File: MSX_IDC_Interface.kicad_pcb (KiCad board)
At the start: 2 copper layers, 103 x 66 mm, 26 parts, among them J1 DE1 GPIO, Q1 2N2222, Q2 2N2222, U1 74LVC245A, U2 74LVC245A, U3 74LVC245A, U4 74LVC245A, U5 74LVC245A, U6 74LS00

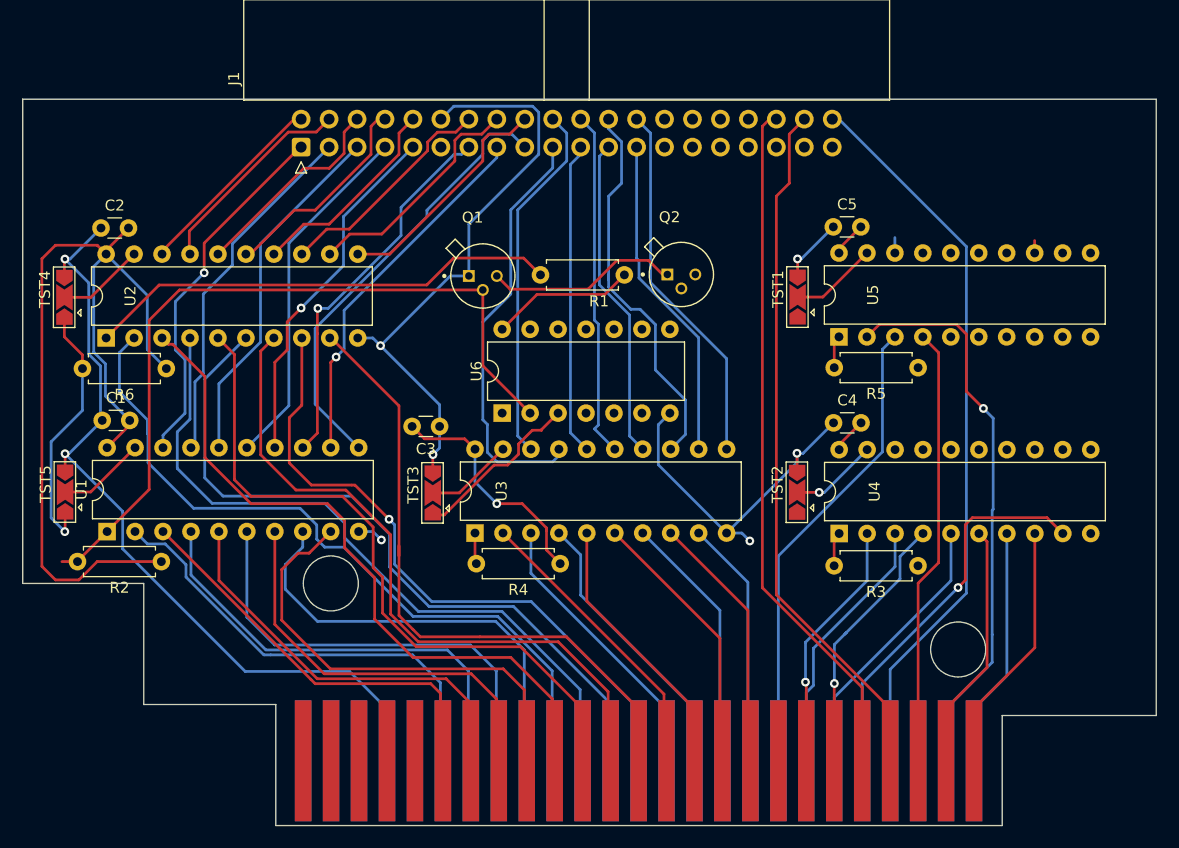
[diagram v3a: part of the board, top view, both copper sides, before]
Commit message: Finished routing. Rules chekc not done yet
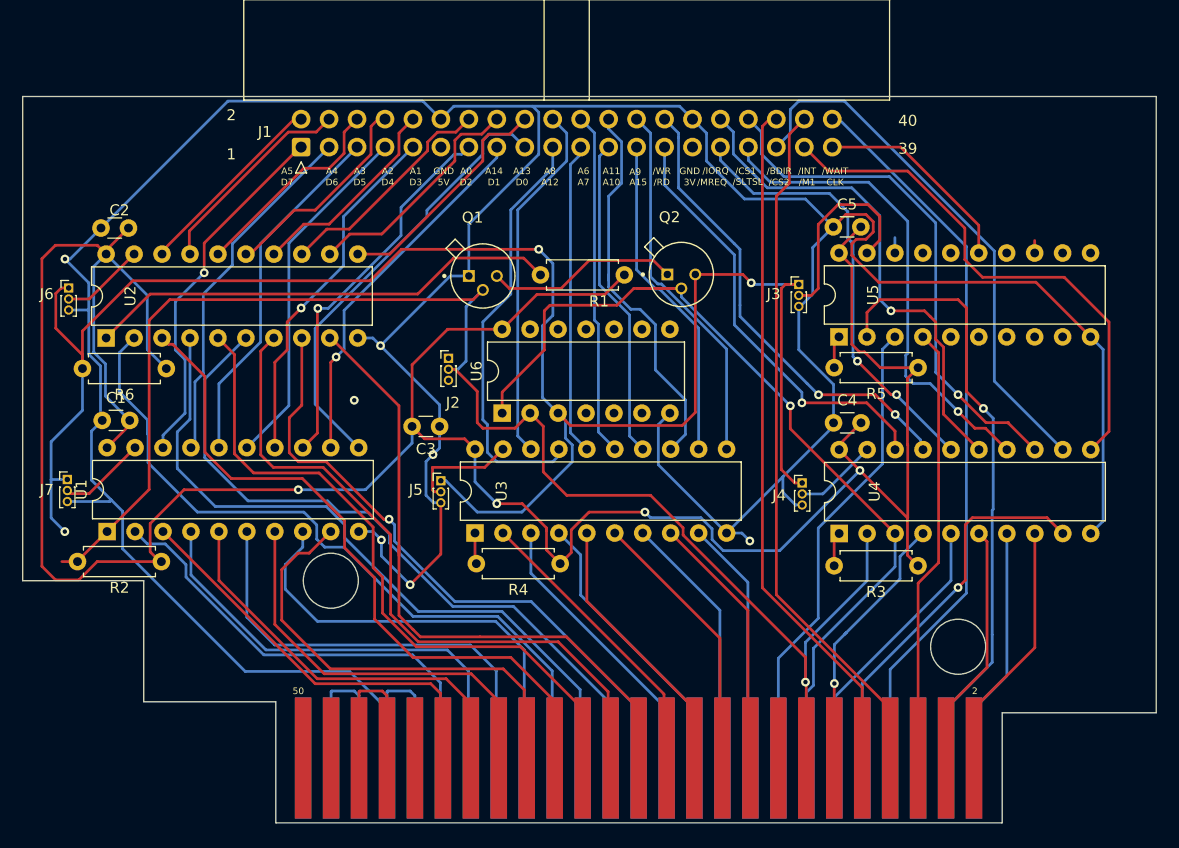
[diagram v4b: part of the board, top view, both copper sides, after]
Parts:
- removed TST1, TST2, TST3, TST4, TST5: SolderJumper_3_Open, Jumper:SolderJumper-3_P2.0mm_Open_TrianglePad1.0x1.5mm
- added J2: Conn_01x03_Male, Connector_PinHeader_1.00mm:PinHeader_1x03_P1.00mm_Vertical, F.Cu at (90.9, 43.9)
- added J3: Conn_01x03_Male, Connector_PinHeader_1.00mm:PinHeader_1x03_P1.00mm_Vertical, F.Cu at (122.7, 37.2)
- added J4: Conn_01x03_Male, Connector_PinHeader_1.00mm:PinHeader_1x03_P1.00mm_Vertical, F.Cu at (123.0, 55.3)
- added J5: Conn_01x03_Male, Connector_PinHeader_1.00mm:PinHeader_1x03_P1.00mm_Vertical, F.Cu at (90.2, 55.1)
- added J6: Conn_01x03_Male, Connector_PinHeader_1.00mm:PinHeader_1x03_P1.00mm_Vertical, F.Cu at (56.3, 37.6)
- added J7: Conn_01x03_Male, Connector_PinHeader_1.00mm:PinHeader_1x03_P1.00mm_Vertical, F.Cu at (56.2, 55.0)
- moved CONN1 0.25 mm to (101.8, 50.7)
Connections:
- net Net-(CONN1-Pad44) renamed SW1
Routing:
- net GNDREF: track 167.9 -> 339.8 mm, vias 8 -> 6
- net Net-(Q2-Pad3): track 39.1 -> 168.0 mm, vias 1 -> 3
- net +3.3V: track 124.3 -> 250.4 mm, vias 1 -> 4
- net /WR: track 24.0 -> 82.5 mm, vias 0 -> 1
- net /C_CS2: track 0.00 -> 49.1 mm
- net /C_M1: track 0.00 -> 48.2 mm
- net /C_CS1: track 0.00 -> 47.6 mm, vias 0 -> 1
- net /RD: track 93.5 -> 140.7 mm
- net /C_IORQ: track 0.00 -> 46.1 mm, vias 0 -> 1
- net /C_SLTSL: track 0.00 -> 44.1 mm, vias 0 -> 1
- net /C_WR: track 0.00 -> 42.8 mm, vias 0 -> 2
- net /C_MREQ: track 0.00 -> 40.5 mm, vias 0 -> 2
- net /C_RD: track 0.00 -> 39.6 mm, vias 0 -> 1
- net C_CLOCK: track 0.00 -> 18.8 mm
- net SW1: track 0.00 -> 14.9 mm
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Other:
- board text added: "/BDIR"
- board text added: "/CS1"
- board text added: "/CS2"
- board text added: "/INT"
- board text added: "/IORQ"
- board text added: "/M1"
- board text added: "/MREQ"
- board text added: "/RD"
- board text added: "/SLTSL"
- board text added: "/WAIT"
- board text added: "/WR"
- board text added: "1"
- board text added: "2"
- board text added: "39"
- board text added: "3V"
- board text added: "40"
- board text added: "49"
- board text added: "50"
- board text added: "5V"
- board text added: "A0"
- board text added: "A1"
- board text added: "A10"
- board text added: "A11"
- board text added: "A12"
- board text added: "A13"
- board text added: "A14"
- board text added: "A15"
- board text added: "A2"
- board text added: "A3"
- board text added: "A4"
- board text added: "A5"
- board text added: "A6"
- board text added: "A7"
- board text added: "A8"
- board text added: "A9"
- board text added: "CLK"
- board text added: "D0"
- board text added: "D1"
- board text added: "D2"
- board text added: "D3"
- board text added: "D4"
- board text added: "D5"
- board text added: "D6"
- board text added: "D7"
- board text added: "GND"

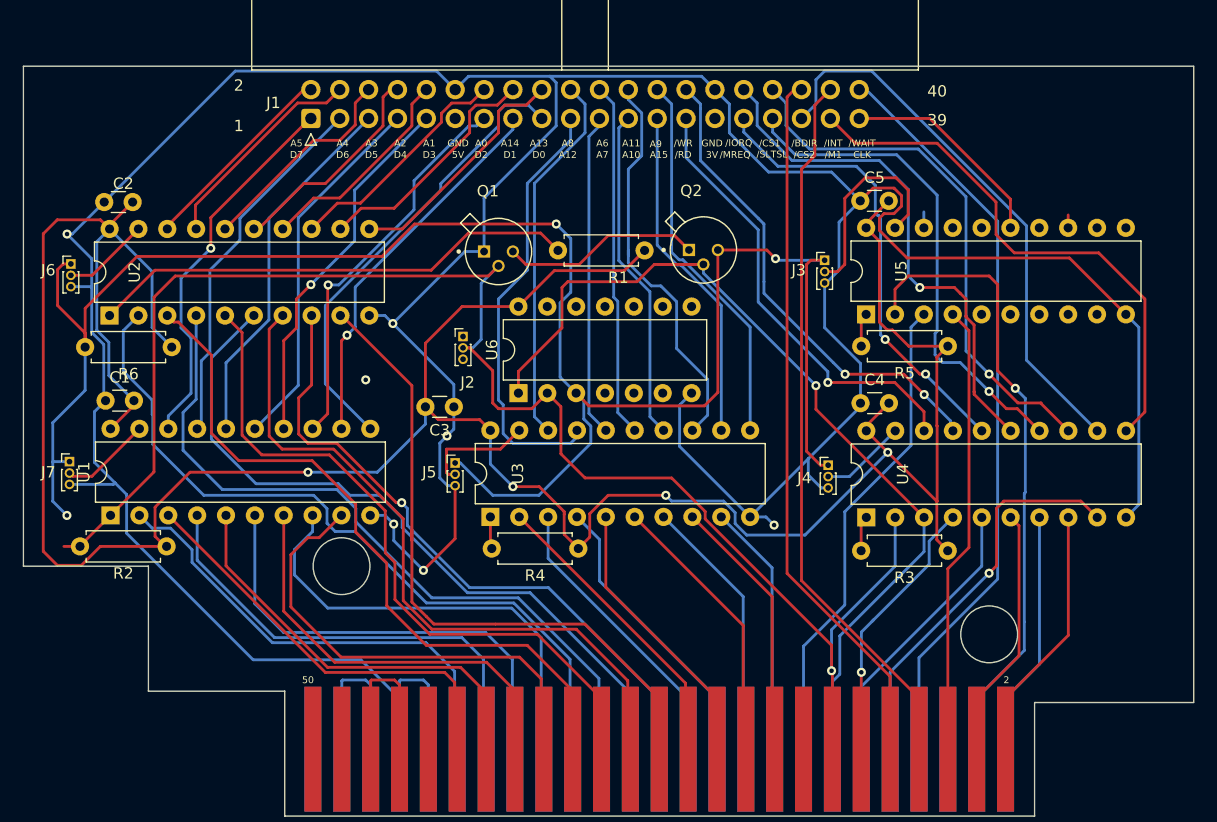
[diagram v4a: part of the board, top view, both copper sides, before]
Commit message: Resolvig clearance issues - wip
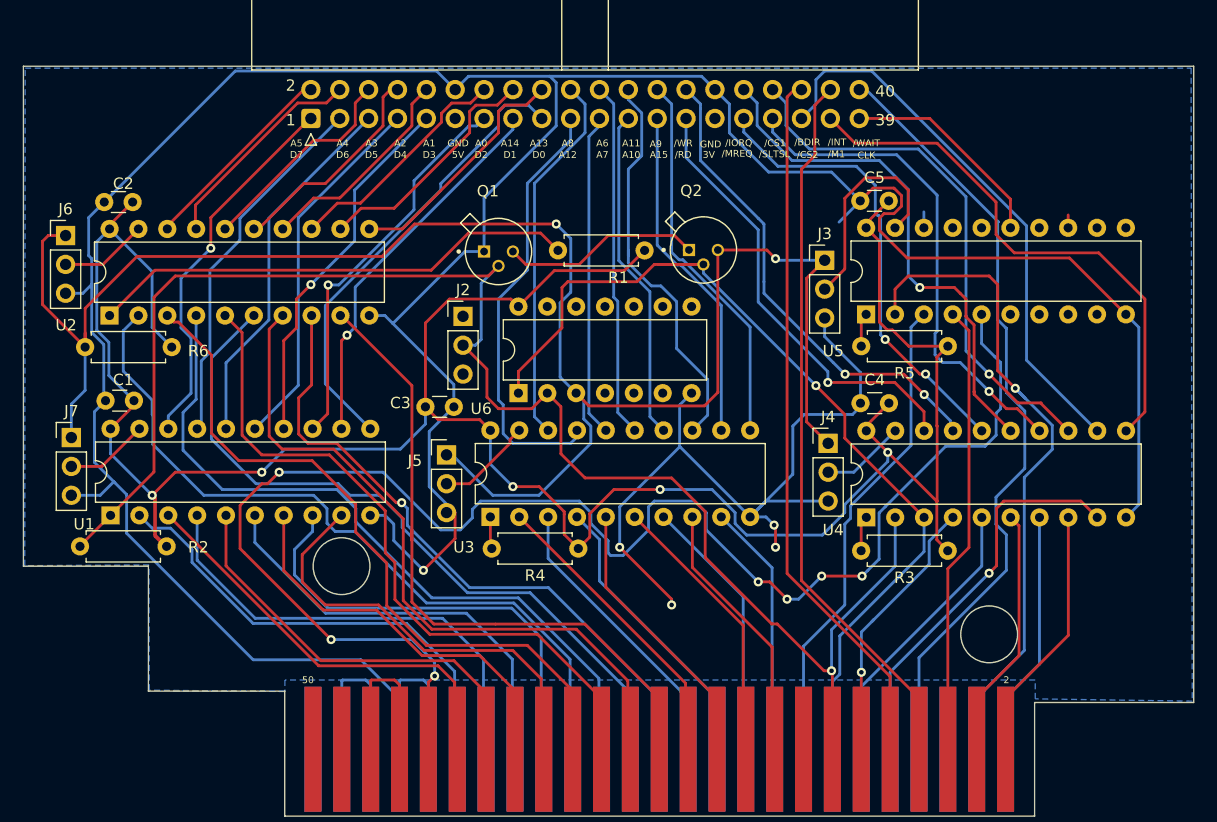
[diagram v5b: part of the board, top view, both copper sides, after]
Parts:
- J2, J3, J4, J5, J6, J7: footprint Connector_PinHeader_1.00mm:PinHeader_1x03_P1.00mm_Vertical -> Connector_PinHeader_2.54mm:PinHeader_1x03_P2.54mm_Vertical
- moved J6 2.54 mm to (55.9, 35.1)
- moved J7 2.13 mm to (56.4, 52.8)
- moved J4 1.92 mm to (123.0, 53.3)
- moved J2 1.77 mm to (90.9, 42.2)
- moved J5 1.04 mm to (89.4, 54.4)
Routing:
- net CLOCK: track 0.00 -> 135.0 mm, vias 0 -> 7
- net +3.3V: track 250.4 -> 219.1 mm, vias 4 -> 5
- net GNDREF: track 339.8 -> 357.1 mm, vias 6 -> 5
- net Net-(Q2-Pad3): track 168.0 -> 161.5 mm, vias 3 -> 2
- net D0: track 41.4 -> 38.1 mm
- net /CS12: track 56.2 -> 59.4 mm
- net D3: track 40.4 -> 37.3 mm
- net /WAIT: track 66.6 -> 69.4 mm
- net D2: track 36.8 -> 34.7 mm
- net Net-(U3-Pad19): track 9.97 -> 8.54 mm
- net /RD: track 140.7 -> 139.8 mm
- net Net-(U5-Pad19): track 18.4 -> 19.3 mm
- net Net-(U2-Pad19): track 7.63 -> 8.38 mm
- net (no net): vias 1 -> 0
- added copper zone on B.Cu, net GNDREF

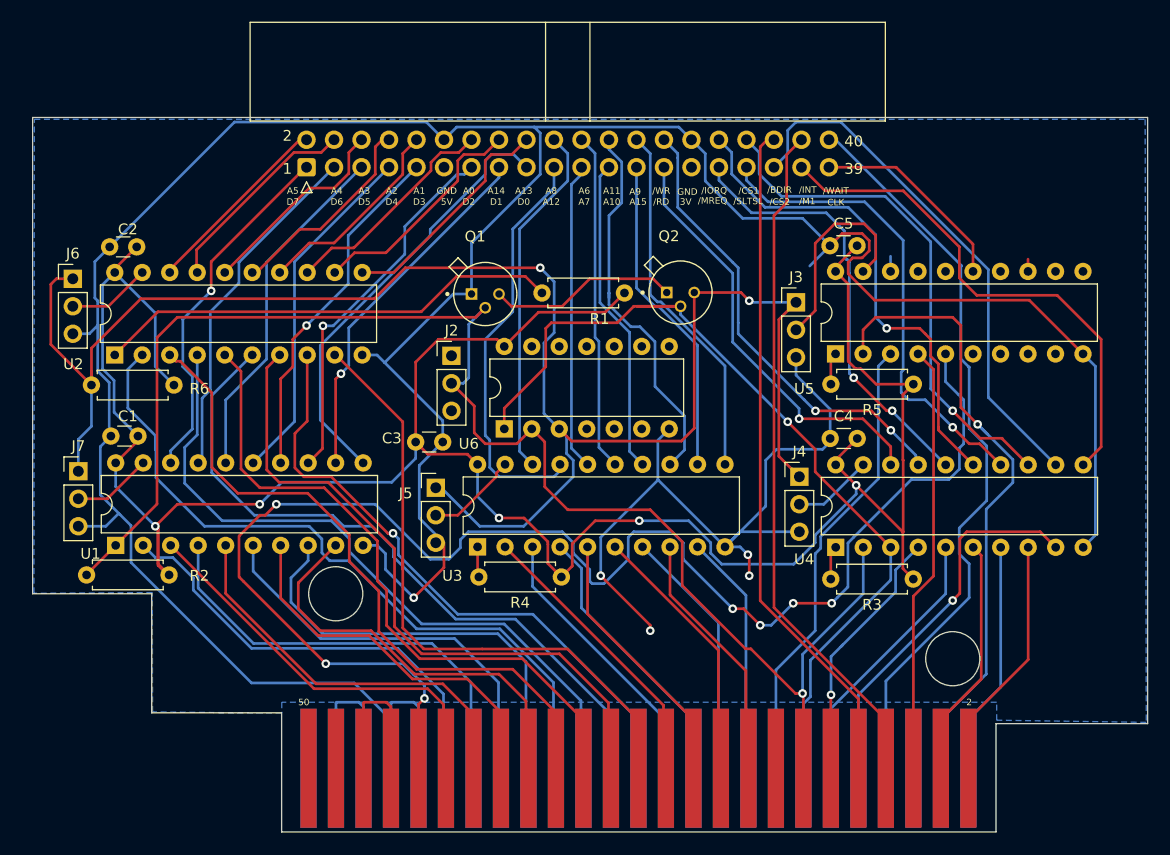
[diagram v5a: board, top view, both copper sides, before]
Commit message: Changed NAND gate for XNOR gate (bug); Completed routing
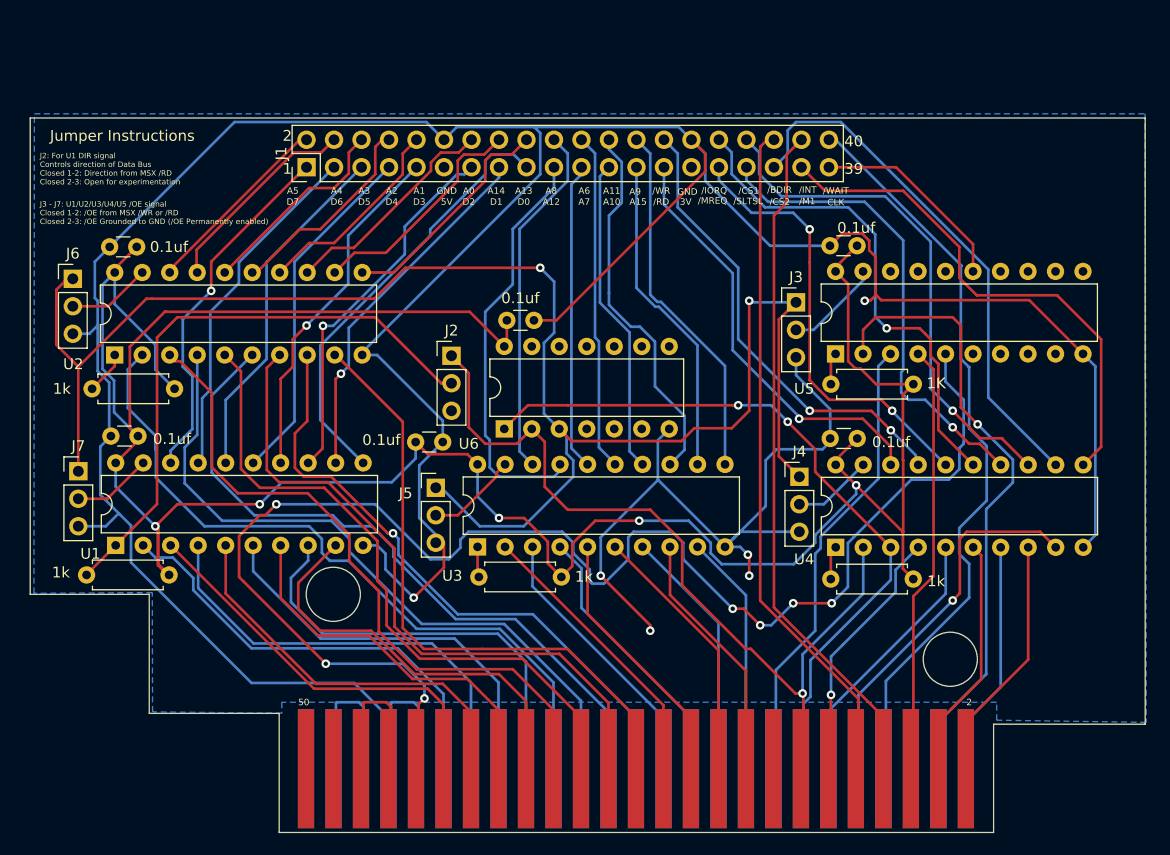
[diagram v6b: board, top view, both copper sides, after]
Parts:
- removed Q1, Q2: 2N2222, Roni Footprints:TO127P584H533-3
- removed R6: 1k, Resistor_THT:R_Axial_DIN0207_L6.3mm_D2.5mm_P7.62mm_Horizontal
- added C6: 0.1uf, Capacitor_THT:C_Disc_D3.0mm_W1.6mm_P2.50mm, F.Cu at (98.5, 38.9)
- J1: footprint Connector_IDC:IDC-Header_2x20_P2.54mm_Horizontal -> Connector_PinHeader_2.54mm:PinHeader_2x20_P2.54mm_Vertical
- R5: value 1k -> 1K
- U6: value 74LS00 -> 4077
- moved R1 42.5 mm to (65.3, 45.2)
- moved CONN1 0.23 mm to (101.6, 50.8)
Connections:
- J2 pad 1: unconnected-(J2-Pad1) -> /RD
- J2 pad 2: /RD -> Net-(J2-Pad2)
- R2 pad 2: /RD -> Net-(J2-Pad2)
- U1 pad 1: /RD -> Net-(J2-Pad2)
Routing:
- net /RD: track 139.8 -> 77.2 mm
- net Net-(J2-Pad2): track 0.00 -> 55.1 mm
- net Net-(R1-Pad2): track 43.1 -> 3.99 mm
- net GNDREF: track 357.1 -> 377.0 mm, vias 5 -> 6
- net +3.3V: track 219.1 -> 237.9 mm
- net Net-(Q1-Pad3): track 18.0 -> 0.00 mm
- net /WR: track 82.5 -> 67.3 mm, vias 1 -> 2
- net Net-(J3-Pad2): track 19.3 -> 9.04 mm
- net Net-(J3-Pad1): track 161.5 -> 154.8 mm
- net /CS12: track 59.4 -> 57.9 mm
- net /C_CS12: track 1.40 -> 0.00 mm
- net unconnected-(U5-Pad13): track 1.13 -> 0.00 mm
- net /C_MREQ: track 40.5 -> 41.2 mm
- net Net-(J6-Pad2): track 8.38 -> 7.70 mm
- net /RFSH: track 40.5 -> 39.9 mm
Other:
- board text added: "J2: For U1 DIR signal Controls direction of Data Bus Closed 1-2: Direction from MSX /RD Closed 2-3: Open for experimentation"
- board text added: "J3 - J7: U1/U2/U3/U4/U5 /OE signal Closed 1-2: /OE from MSX /WR or /RD Closed 2-3: /OE Grounded to GND (/OE Permanently enabled)"
- board text added: "Jumper Instructions"

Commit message: Resistors changed to 2.2k and routing completed
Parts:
- R1, R2, R3, R4: value 1k -> 2.2K
- R5: value 1K -> 2.2K
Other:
- board text added: "J2: U1 DIR signal Closed 1-2: Direction from MSX /RD Closed 2-3: Open for experimentation"
- board text removed: "J2: For U1 DIR signal Controls direction of Data Bus Closed 1-2: Direction from MSX /RD Closed 2-3: Open for experimentation"
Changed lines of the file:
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@@
     (property "Sheetname" "")
     (attr through_hole)
-    (fp_text reference "J1" (at 1.27 -2.33 90) (layer "F.SilkS")
+    (fp_text reference "J1" (at 1.27 -2.33 90) (layer "F.SilkS") hide
       (effects (font (size 1 1) (thickness 0.15)))
     )
@@
       (effects (font (size 1 1) (thickness 0.15)))
     )
-    (fp_text value "1k" (at -2.087435 0.027176) (layer "F.SilkS")
+    (fp_text value "2.2K" (at -3.131533 -0.90199) (layer "F.SilkS")
       (effects (font (size 1 1) (thickness 0.15)))
     )
@@
       (effects (font (size 1 1) (thickness 0.15)))
     )
-    (fp_text value "1K" (at -2.107295 0.085838) (layer "F.SilkS")
+    (fp_text value "2.2K" (at -3.123295 0.085838) (layer "F.SilkS")
       (effects (font (size 1 1) (thickness 0.15)))
     )
@@
       (effects (font (size 1 1) (thickness 0.15)))
     )
-    (fp_text value "1k" (at 9.991748 0.225885) (layer "F.SilkS")
+    (fp_text value "2.2K" (at 10.414 -0.074086) (layer "F.SilkS")
       (effects (font (size 1 1) (thickness 0.15)))
     )
@@
       (effects (font (size 1 1) (thickness 0.15)))
     )
-    (fp_text value "1k" (at -2.116686 -0.201058) (layer "F.SilkS")
+    (fp_text value "2.2K" (at -3.132686 -0.201058) (layer "F.SilkS")
       (effects (font (size 1 1) (thickness 0.15)))
     )
@@
       (effects (font (size 1 1) (thickness 0.15)))
     )
-    (fp_text value "1k" (at 10.414 0) (layer "F.SilkS")
+    (fp_text value "2.2K" (at 10.414 0) (layer "F.SilkS")
       (effects (font (size 1 1) (thickness 0.15)))
     )
@@
     (effects (font (size 0.6 0.6) (thickness 0.11)))
   )
-  (gr_text "J2: For U1 DIR signal\nControls direction of Data Bus\nClosed 1-2: Direction from MSX /RD\nClosed 2-3: Open for experimentation" (at 52.832 24.892) (layer "F.SilkS")
+  (gr_text "J2: U1 DIR signal\nClosed 1-2: Direction from MSX /RD\nClosed 2-3: Open for experimentation" (at 52.832 24.892) (layer "F.SilkS")
     (effects (font (size 0.5 0.5) (thickness 0.125)) (justify left))
   )
@@
     (effects (font (size 0.6 0.6) (thickness 0.11)))
   )
-  (gr_text "A5" (at 76.2 26.924) (layer "F.SilkS")
-    (effects (font (size 0.6 0.6) (thickness 0.11)))
-  )
-  (gr_text "D7" (at 76.2 27.94) (layer "F.SilkS")
-    (effects (font (size 0.6 0.6) (thickness 0.11)))
-  )
+  (gr_text "A5" (at 77.216 26.924) (layer "F.SilkS")
+    (effects (font (size 0.6 0.6) (thickness 0.11)))
+  )
+  (gr_text "D7" (at 77.216 27.94) (layer "F.SilkS")
+    (effects (font (size 0.6 0.6) (thickness 0.11)))
+  )

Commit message: Added silkscreen to pcb
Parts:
- added CD4077 / XNOR Truth Table: LOGO, LOGO, B.Cu at (143.1, 27.4)
- added G***: LOGO, LOGO, F.Cu at (142.9, 26.7)
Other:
- board text added: "RCC @ 2022"
- board text added: "https://www.facebook.com/groups/retrocpu"
